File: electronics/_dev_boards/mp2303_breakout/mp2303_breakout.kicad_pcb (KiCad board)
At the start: 2 copper layers, 30 x 30 mm, 18 parts, among them J1 CONN_01X03, J2 CONN_01X02, P1 SYMBOL, U1 MP2303

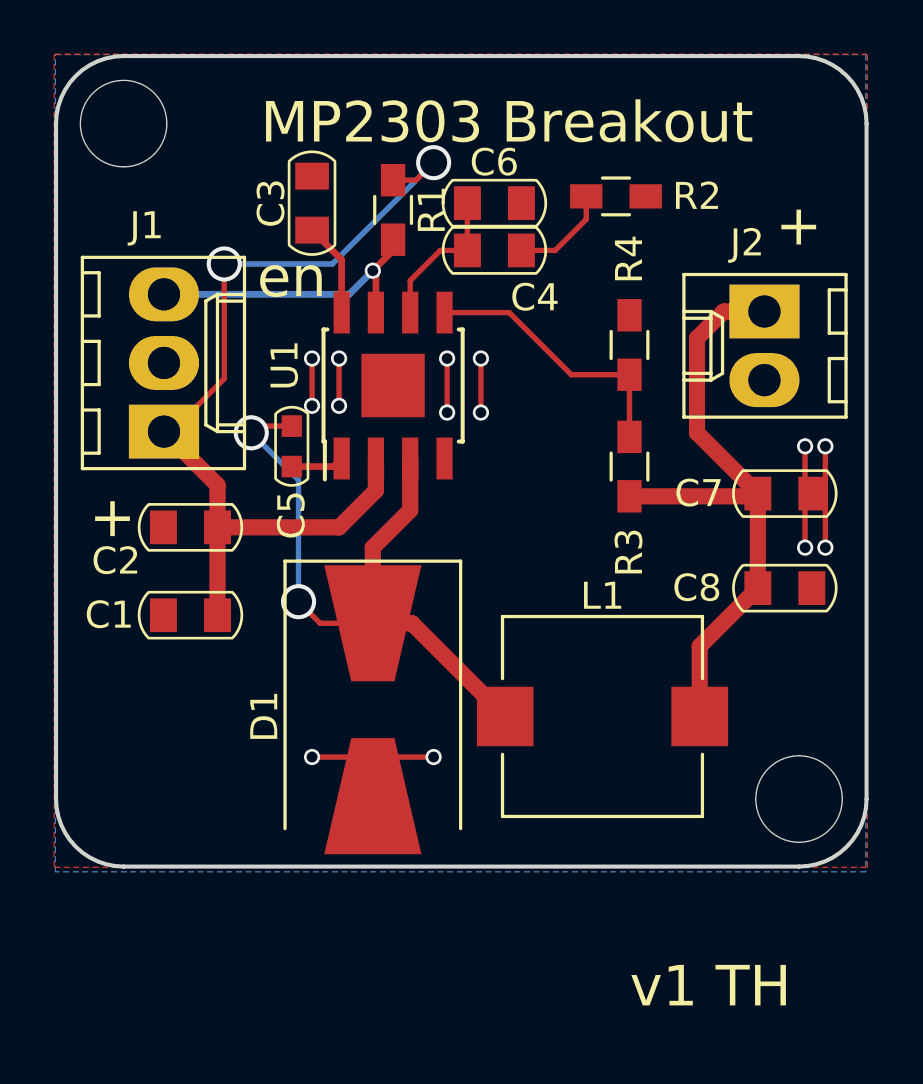
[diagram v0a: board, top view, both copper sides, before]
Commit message: Finish up MP23xx board
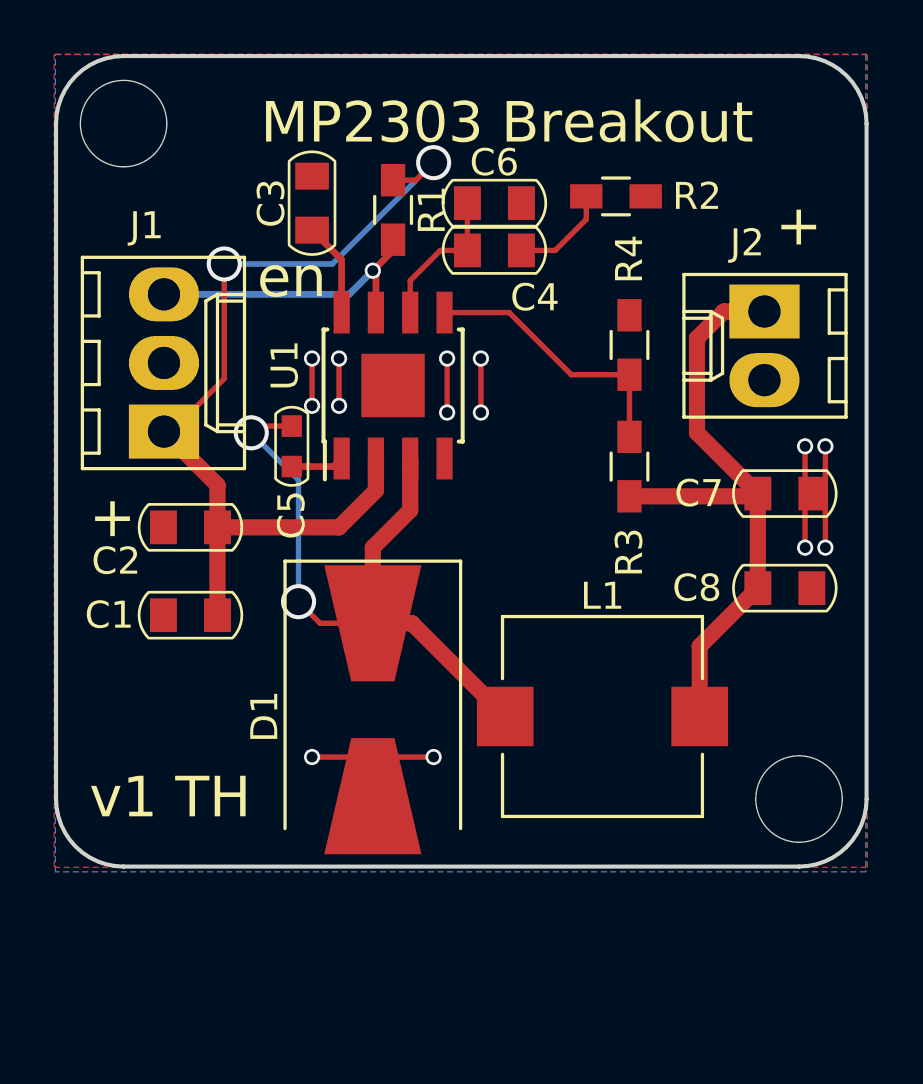
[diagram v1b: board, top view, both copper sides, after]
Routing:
- net GND: track 19.5 -> 0.00 mm, vias 14 -> 0
- net (no net): track 0.00 -> 19.5 mm, vias 0 -> 14
